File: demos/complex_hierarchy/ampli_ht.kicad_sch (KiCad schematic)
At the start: 29 parts, among them P3 CONN_2, P4 CONN_2, Q1 MPSA92, Q2 MPSA42, Q3 MPSA92, Q4 MPSA42, U3 LM358N

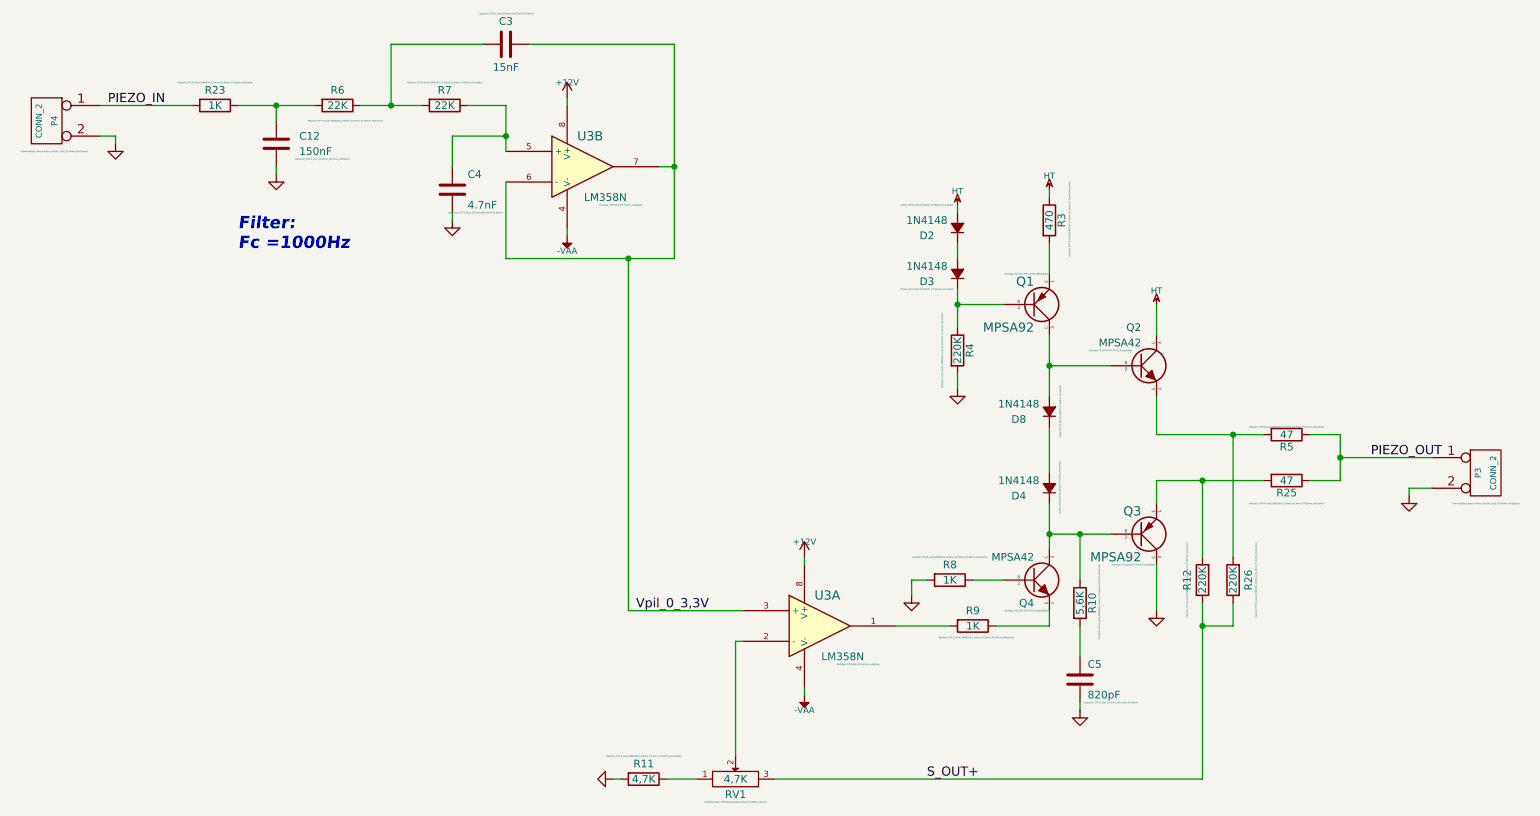
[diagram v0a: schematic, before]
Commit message: feat: update kicad to 9.0.0+dfsg-1
Signed-off-by: lhdjply <lhdjply@126.com>
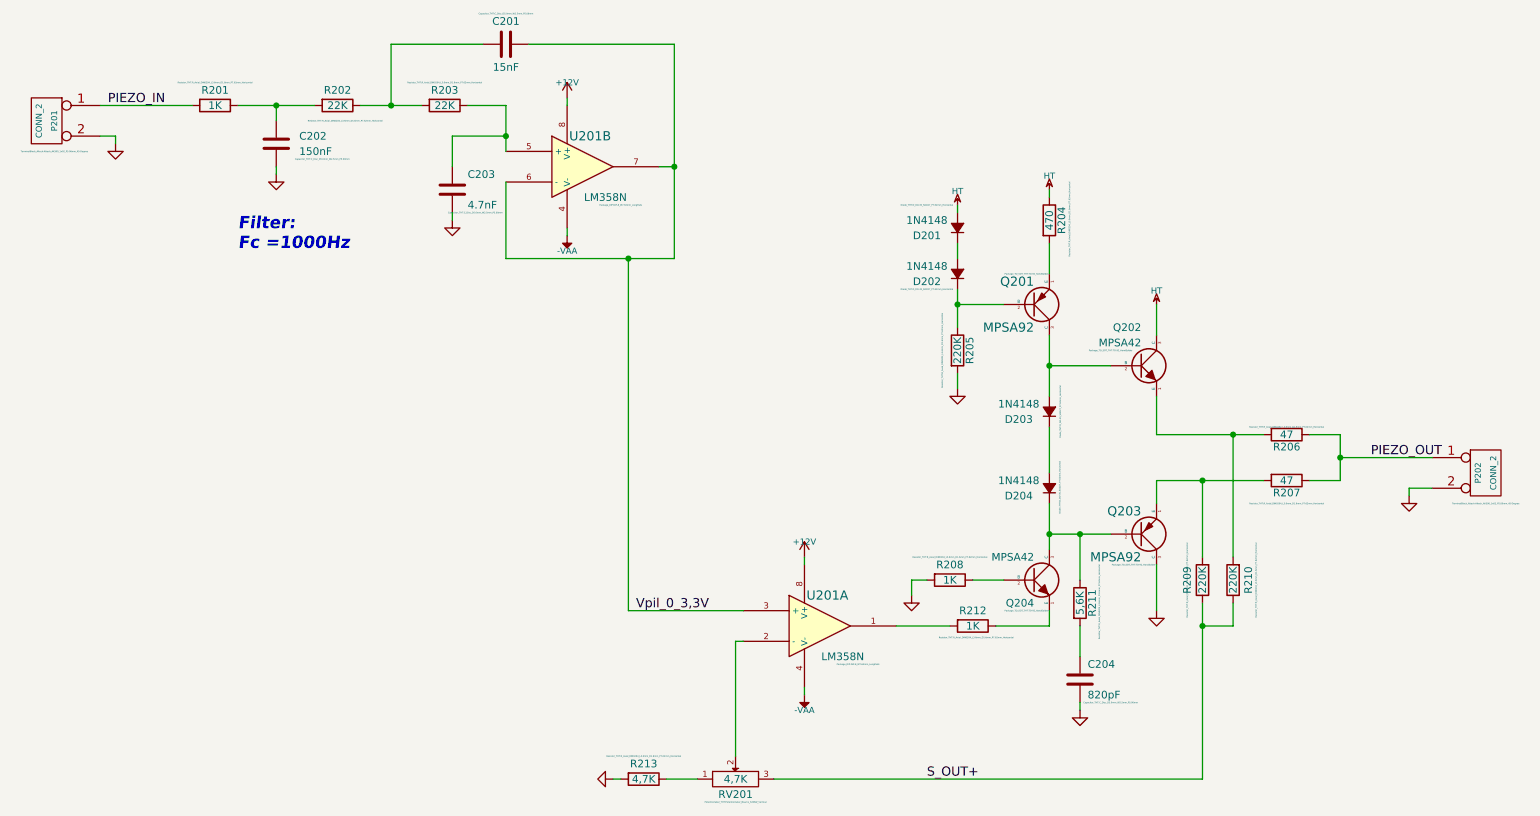
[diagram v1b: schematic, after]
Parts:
- C201: renamed from C3; symbol complex_hierarchy_schlib:C -> complex_hierarchy:C
- C202: renamed from C12; symbol complex_hierarchy_schlib:C -> complex_hierarchy:C
- C203: renamed from C4; symbol complex_hierarchy_schlib:C -> complex_hierarchy:C
- C204: renamed from C5; symbol complex_hierarchy_schlib:C -> complex_hierarchy:C
- D201: renamed from D2; symbol complex_hierarchy_schlib:D_Small -> complex_hierarchy:D_Small
- D202: renamed from D3; symbol complex_hierarchy_schlib:D_Small -> complex_hierarchy:D_Small
- D203: renamed from D8; symbol complex_hierarchy_schlib:D_Small -> complex_hierarchy:D_Small
- D204: renamed from D4; symbol complex_hierarchy_schlib:D_Small -> complex_hierarchy:D_Small
- P201: renamed from P4; symbol complex_hierarchy_schlib:CONN_2 -> complex_hierarchy:CONN_2
- P202: renamed from P3; symbol complex_hierarchy_schlib:CONN_2 -> complex_hierarchy:CONN_2
- Q201: renamed from Q1; symbol complex_hierarchy_schlib:MPSA92 -> complex_hierarchy:MPSA92
- Q202: renamed from Q2; symbol complex_hierarchy_schlib:MPSA42 -> complex_hierarchy:MPSA42
- Q203: renamed from Q3; symbol complex_hierarchy_schlib:MPSA92 -> complex_hierarchy:MPSA92
- Q204: renamed from Q4; symbol complex_hierarchy_schlib:MPSA42 -> complex_hierarchy:MPSA42
- R201: renamed from R23; symbol complex_hierarchy_schlib:R -> complex_hierarchy:R
- R202: renamed from R6; symbol complex_hierarchy_schlib:R -> complex_hierarchy:R
- R203: renamed from R7; symbol complex_hierarchy_schlib:R -> complex_hierarchy:R
- R204: renamed from R3; symbol complex_hierarchy_schlib:R -> complex_hierarchy:R
- R205: renamed from R4; symbol complex_hierarchy_schlib:R -> complex_hierarchy:R
- R206: renamed from R5; symbol complex_hierarchy_schlib:R -> complex_hierarchy:R
- R207: renamed from R25; symbol complex_hierarchy_schlib:R -> complex_hierarchy:R
- R208: renamed from R8; symbol complex_hierarchy_schlib:R -> complex_hierarchy:R
- R209: renamed from R12; symbol complex_hierarchy_schlib:R -> complex_hierarchy:R
- R210: renamed from R26; symbol complex_hierarchy_schlib:R -> complex_hierarchy:R
- R211: renamed from R10; symbol complex_hierarchy_schlib:R -> complex_hierarchy:R
- R212: renamed from R9; symbol complex_hierarchy_schlib:R -> complex_hierarchy:R
- R213: renamed from R11; symbol complex_hierarchy_schlib:R -> complex_hierarchy:R
- RV201: renamed from RV1; symbol complex_hierarchy_schlib:POT -> complex_hierarchy:POT
- U201: renamed from U3; symbol complex_hierarchy_schlib:LM358N -> complex_hierarchy:LM358N
